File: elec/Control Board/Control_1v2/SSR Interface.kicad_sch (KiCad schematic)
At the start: 21 parts, among them J11 Screw_Terminal_01x02, Q601 BSS138

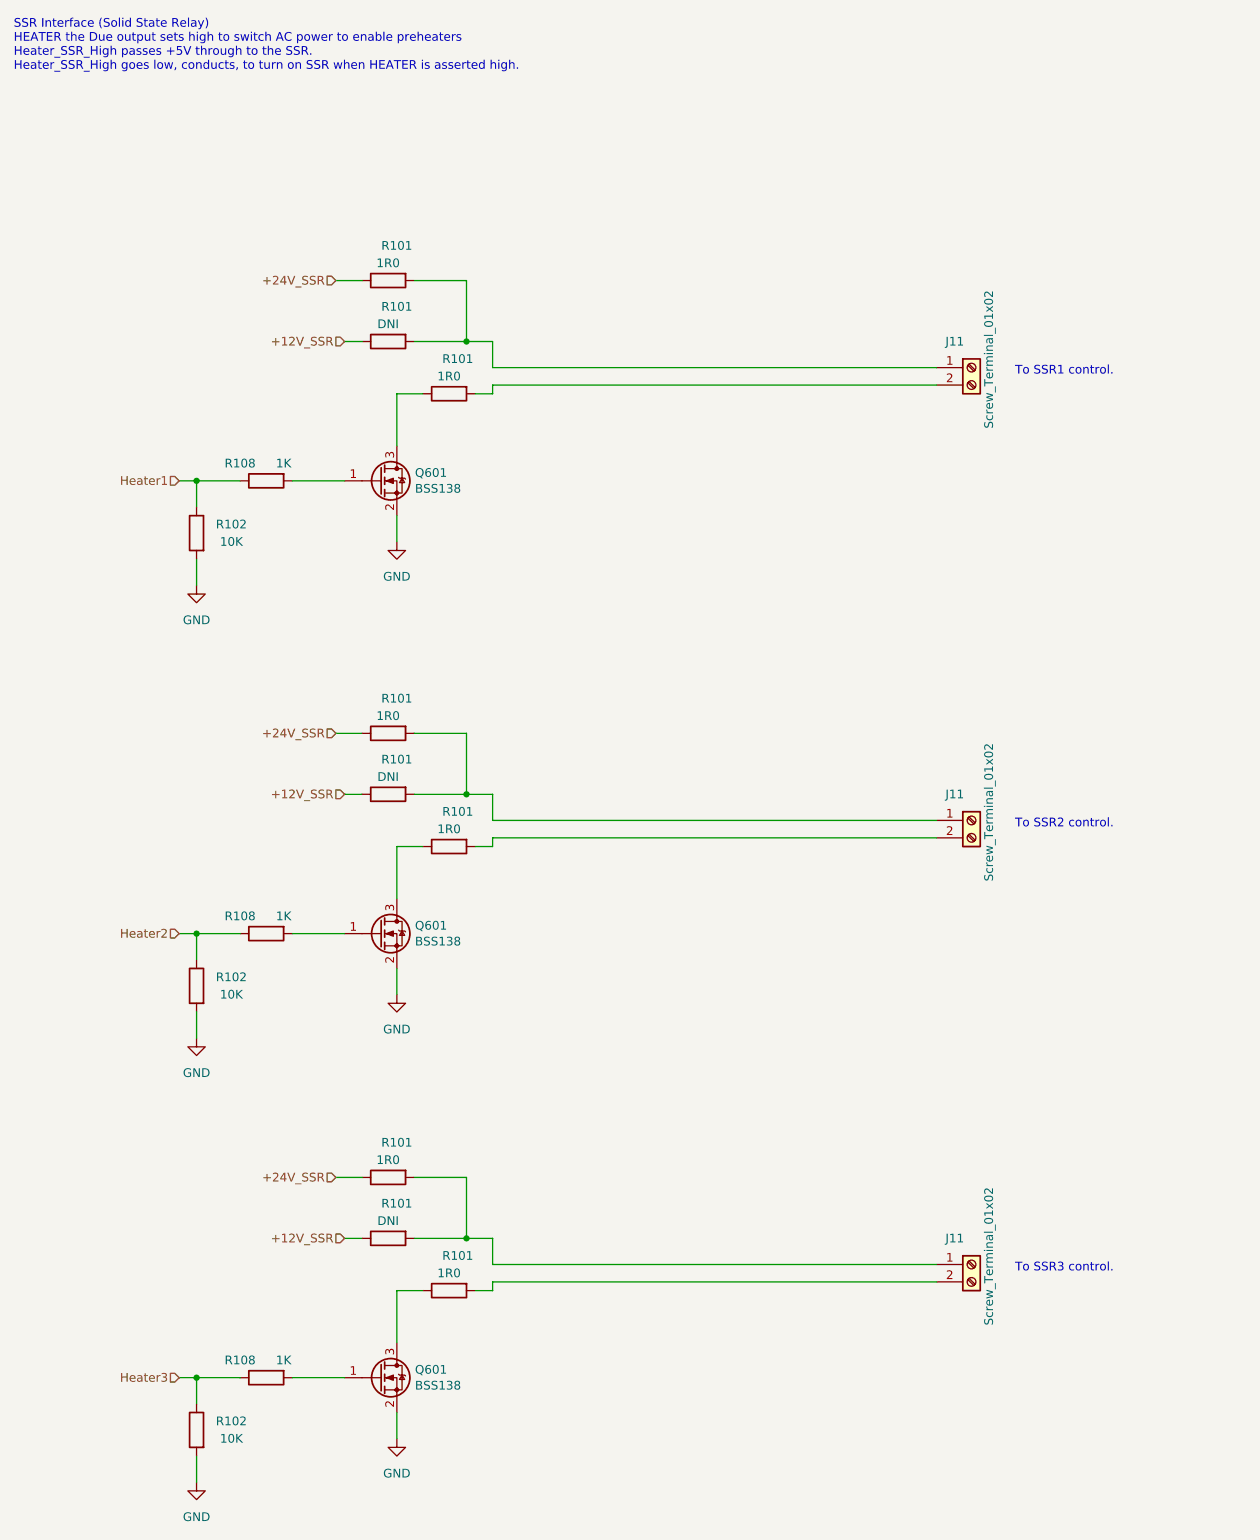
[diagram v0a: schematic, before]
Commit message: Update Control_1v2.kicad_sch for correct JLCPCB part number on JST 2 pin XH Connector. Wire up J30 as connector for OEDCS Fan.
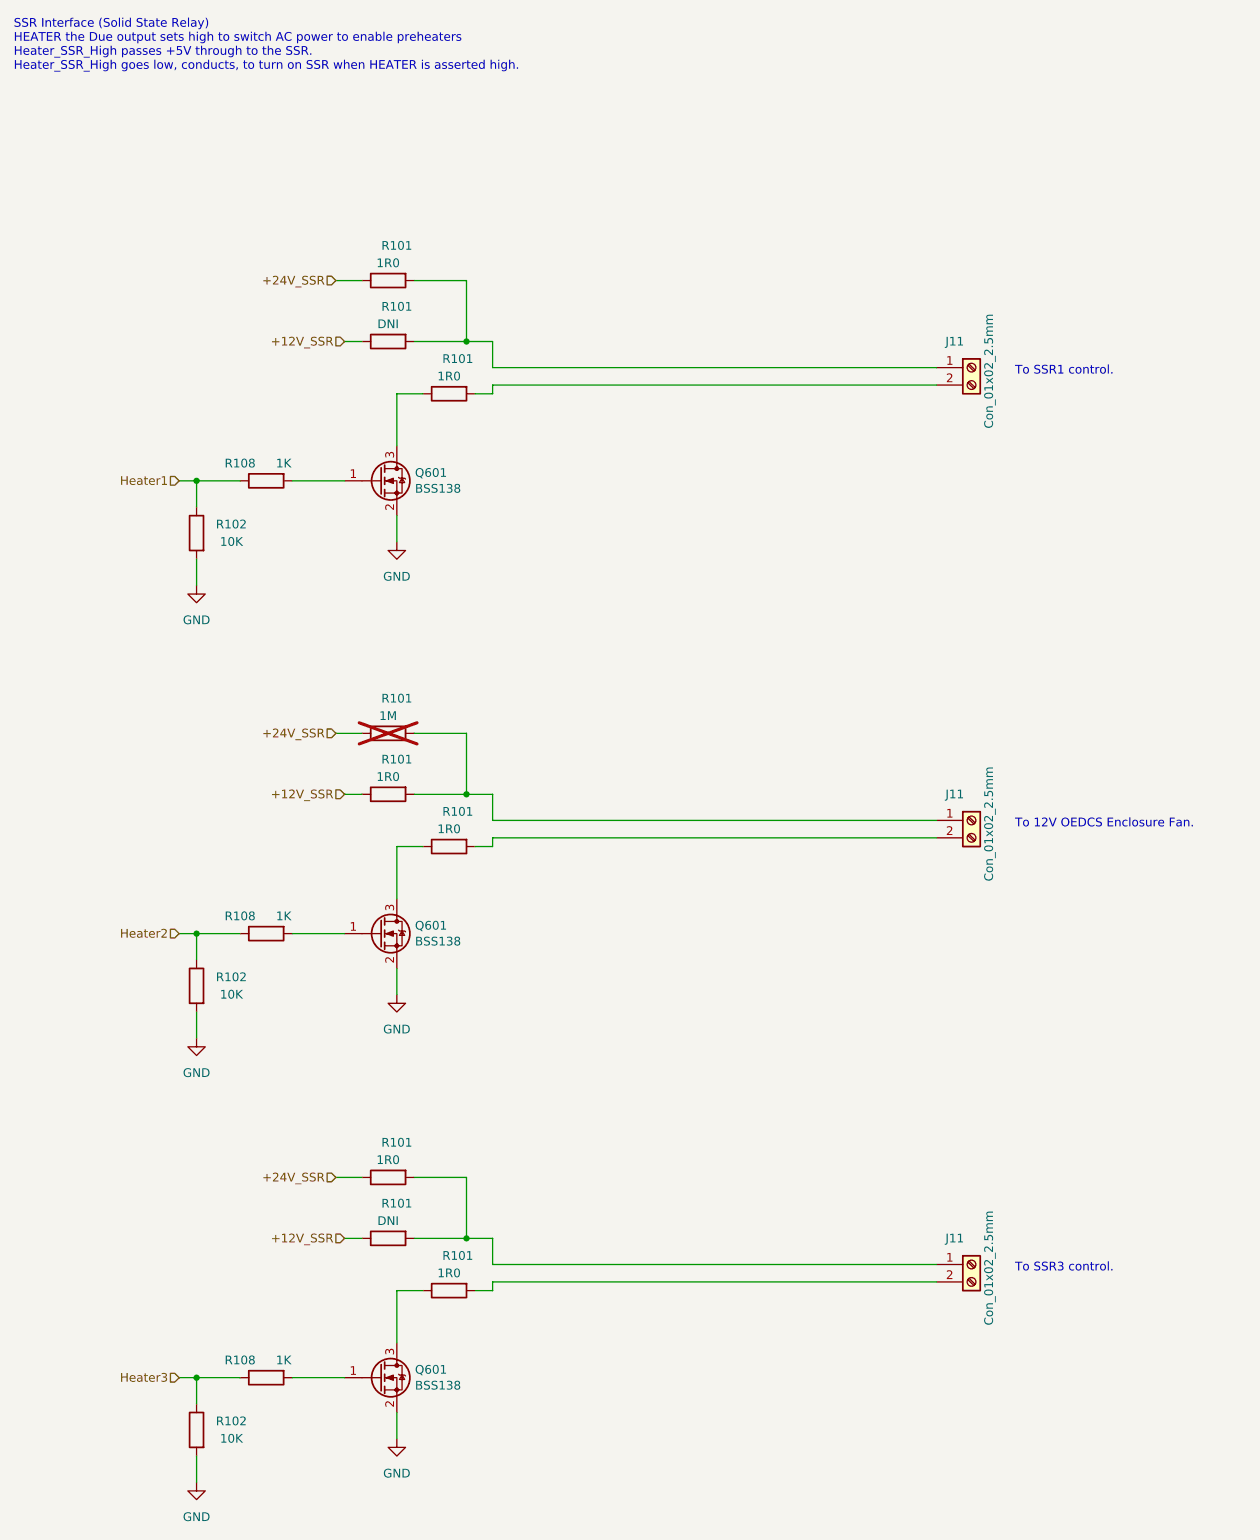
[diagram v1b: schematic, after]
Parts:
- J11: value Screw_Terminal_01x02 -> Con_01x02_2.5mm; footprint TerminalBlock_TE-Connectivity:TerminalBlock_TE_282834-2_1x02_P2.54mm_Horizontal -> Connector_JST:JST_XH_B2B-XH-AM_1x02_P2.50mm_Vertical; Cost 0.1537 -> 0.2156; MPN DB125-2.54-2P-GN-S -> B2B-XH-A-GU; Manufacturer DIBO -> JST
- R101: value DNI -> 1R0; Distributor 1 (none) -> JLCPCB; Distributor 1 PN (none) -> C269434
- R101: value 1R0 -> 1M; Distributor 1 PN C269434 -> (none); now not fitted
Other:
- note added: "To 12V OEDCS Enclosure Fan."
- note removed: "To SSR2 control."
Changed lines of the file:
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@@
     )
   )
-  (text "To SSR2 control." (at 210.82 151.13 0)
+  (text "To 12V OEDCS Enclosure Fan." (at 210.82 151.13 0)
     (effects (font (size 1.27 1.27)) (justify left bottom))
   )
@@
       (effects (font (size 1.27 1.27)) (justify left))
     )
-    (property "Value" "Screw_Terminal_01x02" (at 207.01 92.71 90)
+    (property "Value" "Con_01x02_2.5mm" (at 207.01 92.71 90)
       (effects (font (size 1.27 1.27)) (justify left))
     )
-    (property "Footprint" "TerminalBlock_TE-Connectivity:TerminalBlock_TE_282834-2_1x02_P2.54mm_Horizontal" (at 204.47 83.82 0)
+    (property "Footprint" "Connector_JST:JST_XH_B2B-XH-AM_1x02_P2.50mm_Vertical" (at 204.47 83.82 0)
       (effects (font (size 1.27 1.27)) hide)
     )
@@
       (effects (font (size 1.27 1.27)) hide)
     )
-    (property "Cost" "0.1537" (at 204.47 83.82 0)
-      (effects (font (size 1.27 1.27)) hide)
-    )
-    (property "Description" "1x2P XH 1 2.5mm 2 Brass Plugin,P=2.5mm Wire To Board / Wire To Wire Connector ROHS" (at 204.47 83.82 0)
+    (property "Cost" "0.2156" (at 204.47 83.82 0)
+      (effects (font (size 1.27 1.27)) hide)
+    )
+    (property "Description" "1x2P 2P XH Gold 2 -25℃~+85℃ 3A 1 2.5mm Brass Direct Insert Plugin,P=2.5mm Wire To Board Connector ROHS" (at 204.47 83.82 0)
       (effects (font (size 1.27 1.27)) hide)
     )
@@
       (effects (font (size 1.27 1.27)) hide)
     )
-    (property "MPN" "DB125-2.54-2P-GN-S" (at 204.47 83.82 0)
-      (effects (font (size 1.27 1.27)) hide)
-    )
-    (property "Manufacturer" "DIBO" (at 204.47 83.82 0)
+    (property "MPN" "B2B-XH-A-GU" (at 204.47 83.82 0)
+      (effects (font (size 1.27 1.27)) hide)
+    )
+    (property "Manufacturer" "JST" (at 204.47 83.82 0)
       (effects (font (size 1.27 1.27)) hide)
     )
@@
       (effects (font (size 1.27 1.27)))
     )
-    (property "Value" "DNI" (at 119.38 143.51 90)
+    (property "Value" "1R0" (at 119.38 143.51 90)
       (effects (font (size 1.27 1.27)))
     )
@@
       (effects (font (size 1.27 1.27)) hide)
     )
-    (property "Distributor 1" "" (at 119.38 146.05 90)
-      (effects (font (size 1.27 1.27)) hide)
-    )
-    (property "Distributor 1 PN" "" (at 119.38 146.05 90)
+    (property "Distributor 1" "JLCPCB" (at 119.38 146.05 90)
+      (effects (font (size 1.27 1.27)) hide)
+    )
+    (property "Distributor 1 PN" "C269434" (at 119.38 146.05 90)
       (effects (font (size 1.27 1.27)) hide)
     )
@@
       (effects (font (size 1.27 1.27)) (justify left))
     )
-    (property "Value" "Screw_Terminal_01x02" (at 207.01 158.75 90)
+    (property "Value" "Con_01x02_2.5mm" (at 207.01 158.75 90)
       (effects (font (size 1.27 1.27)) (justify left))
     )
-    (property "Footprint" "TerminalBlock_TE-Connectivity:TerminalBlock_TE_282834-2_1x02_P2.54mm_Horizontal" (at 204.47 149.86 0)
+    (property "Footprint" "Connector_JST:JST_XH_B2B-XH-AM_1x02_P2.50mm_Vertical" (at 204.47 149.86 0)
       (effects (font (size 1.27 1.27)) hide)
     )
@@
       (effects (font (size 1.27 1.27)) hide)
     )
-    (property "Cost" "0.1537" (at 204.47 149.86 0)
-      (effects (font (size 1.27 1.27)) hide)
-    )
-    (property "Description" "1x2P XH 1 2.5mm 2 Brass Plugin,P=2.5mm Wire To Board / Wire To Wire Connector ROHS" (at 204.47 149.86 0)
+    (property "Cost" "0.2156" (at 204.47 149.86 0)
+      (effects (font (size 1.27 1.27)) hide)
+    )
+    (property "Description" "1x2P 2P XH Gold 2 -25℃~+85℃ 3A 1 2.5mm Brass Direct Insert Plugin,P=2.5mm Wire To Board Connector ROHS" (at 204.47 149.86 0)
       (effects (font (size 1.27 1.27)) hide)
     )
@@
       (effects (font (size 1.27 1.27)) hide)
     )
-    (property "MPN" "DB125-2.54-2P-GN-S" (at 204.47 149.86 0)
-      (effects (font (size 1.27 1.27)) hide)
-    )
-    (property "Manufacturer" "DIBO" (at 204.47 149.86 0)
+    (property "MPN" "B2B-XH-A-GU" (at 204.47 149.86 0)
+      (effects (font (size 1.27 1.27)) hide)
+    )
+    (property "Manufacturer" "JST" (at 204.47 149.86 0)
       (effects (font (size 1.27 1.27)) hide)
     )
@@
   )
   (symbol (lib_id "Device:R") (at 119.38 137.16 90) (mirror x) (unit 1)
-    (in_bom yes) (on_board yes) (dnp no)
+    (in_bom yes) (on_board yes) (dnp yes)
     (property "Reference" "R101" (at 120.65 132.08 90)
       (effects (font (size 1.27 1.27)))
     )
-    (property "Value" "1R0" (at 119.38 134.62 90)
+    (property "Value" "1M" (at 119.38 134.62 90)
       (effects (font (size 1.27 1.27)))
     )
@@
       (effects (font (size 1.27 1.27)) hide)
     )
-    (property "Distributor 1 PN" "C269434" (at 119.38 137.16 90)
+    (property "Distributor 1 PN" "" (at 119.38 137.16 90)
       (effects (font (size 1.27 1.27)) hide)
     )
@@
       (effects (font (size 1.27 1.27)) hide)
     )
-    (property "Description" "0.1W ±5% 1Ω 0603 Chip Resistor - Surface Mount ROHS" (at 119.38 137.16 0)
+    (property "Description" "" (at 119.38 137.16 0)
       (effects (font (size 1.27 1.27)) hide)
     )
@@
       (effects (font (size 1.27 1.27)) (justify left))
     )
-    (property "Value" "Screw_Terminal_01x02" (at 207.01 223.52 90)
+    (property "Value" "Con_01x02_2.5mm" (at 207.01 223.52 90)
       (effects (font (size 1.27 1.27)) (justify left))
     )
-    (property "Footprint" "TerminalBlock_TE-Connectivity:TerminalBlock_TE_282834-2_1x02_P2.54mm_Horizontal" (at 204.47 214.63 0)
+    (property "Footprint" "Connector_JST:JST_XH_B2B-XH-AM_1x02_P2.50mm_Vertical" (at 204.47 214.63 0)
       (effects (font (size 1.27 1.27)) hide)
     )
@@
       (effects (font (size 1.27 1.27)) hide)
     )
-    (property "Cost" "0.1537" (at 204.47 214.63 0)
-      (effects (font (size 1.27 1.27)) hide)
-    )
-    (property "Description" "1x2P XH 1 2.5mm 2 Brass Plugin,P=2.5mm Wire To Board / Wire To Wire Connector ROHS" (at 204.47 214.63 0)
+    (property "Cost" "0.2156" (at 204.47 214.63 0)
+      (effects (font (size 1.27 1.27)) hide)
+    )
+    (property "Description" "1x2P 2P XH Gold 2 -25℃~+85℃ 3A 1 2.5mm Brass Direct Insert Plugin,P=2.5mm Wire To Board Connector ROHS" (at 204.47 214.63 0)
       (effects (font (size 1.27 1.27)) hide)
     )
@@
       (effects (font (size 1.27 1.27)) hide)
     )
-    (property "MPN" "DB125-2.54-2P-GN-S" (at 204.47 214.63 0)
-      (effects (font (size 1.27 1.27)) hide)
-    )
-    (property "Manufacturer" "DIBO" (at 204.47 214.63 0)
-      (effects (font (size 1.27 1.27)) hide)
-    )
+    (property "MPN" "B2B-XH-A-GU" (at 204.47 214.63 0)
+      (effects (font (size 1.27 1.27)) hide)
+    )
+    (property "Manufacturer" "JST" (at 204.47 214.63 0)
+      (effects (font (size 1.27 1.27)) hide)
+    )

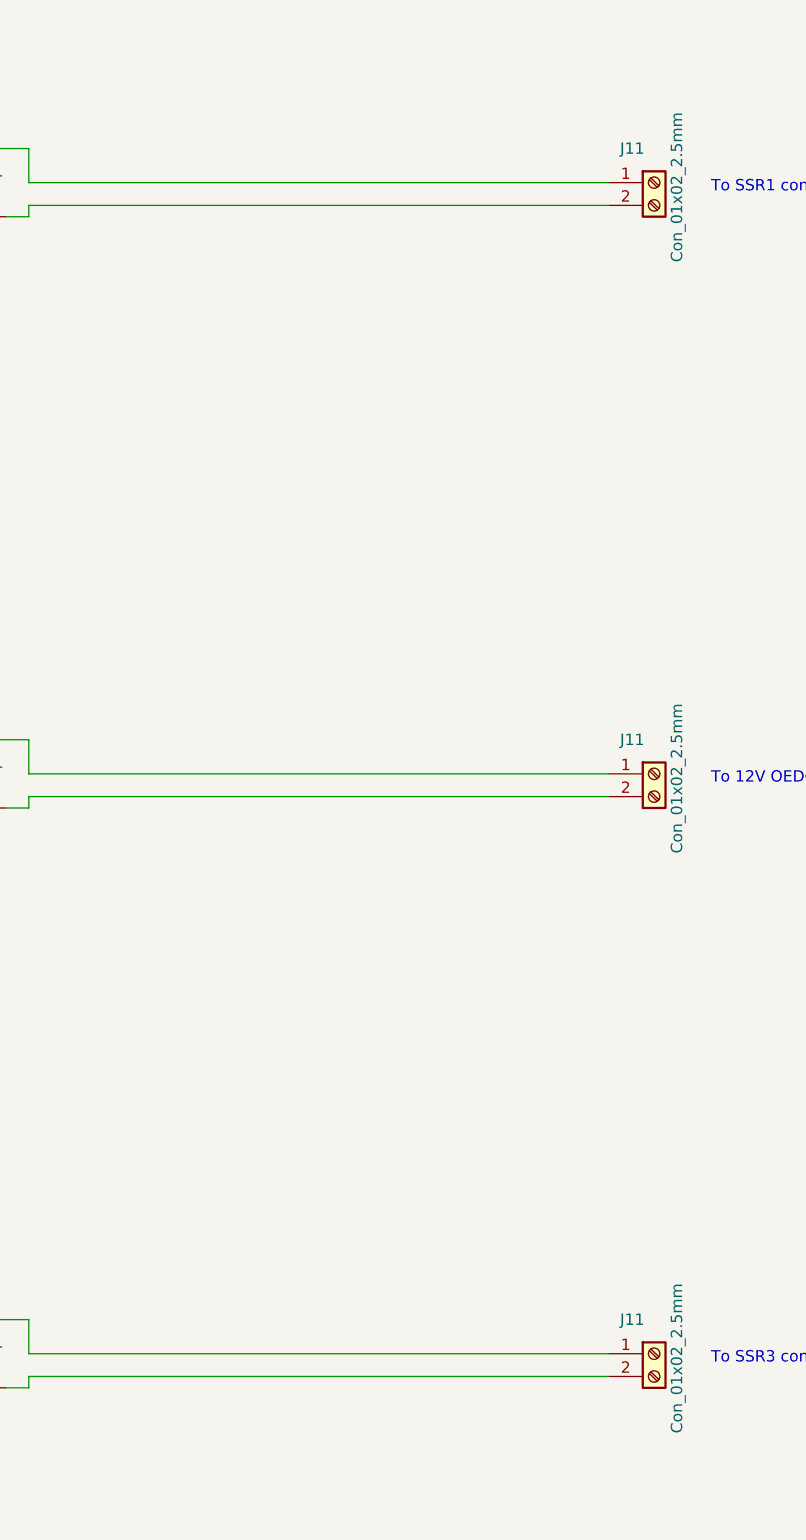
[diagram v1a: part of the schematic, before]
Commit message: PCB V1.2. Routing with out errors.
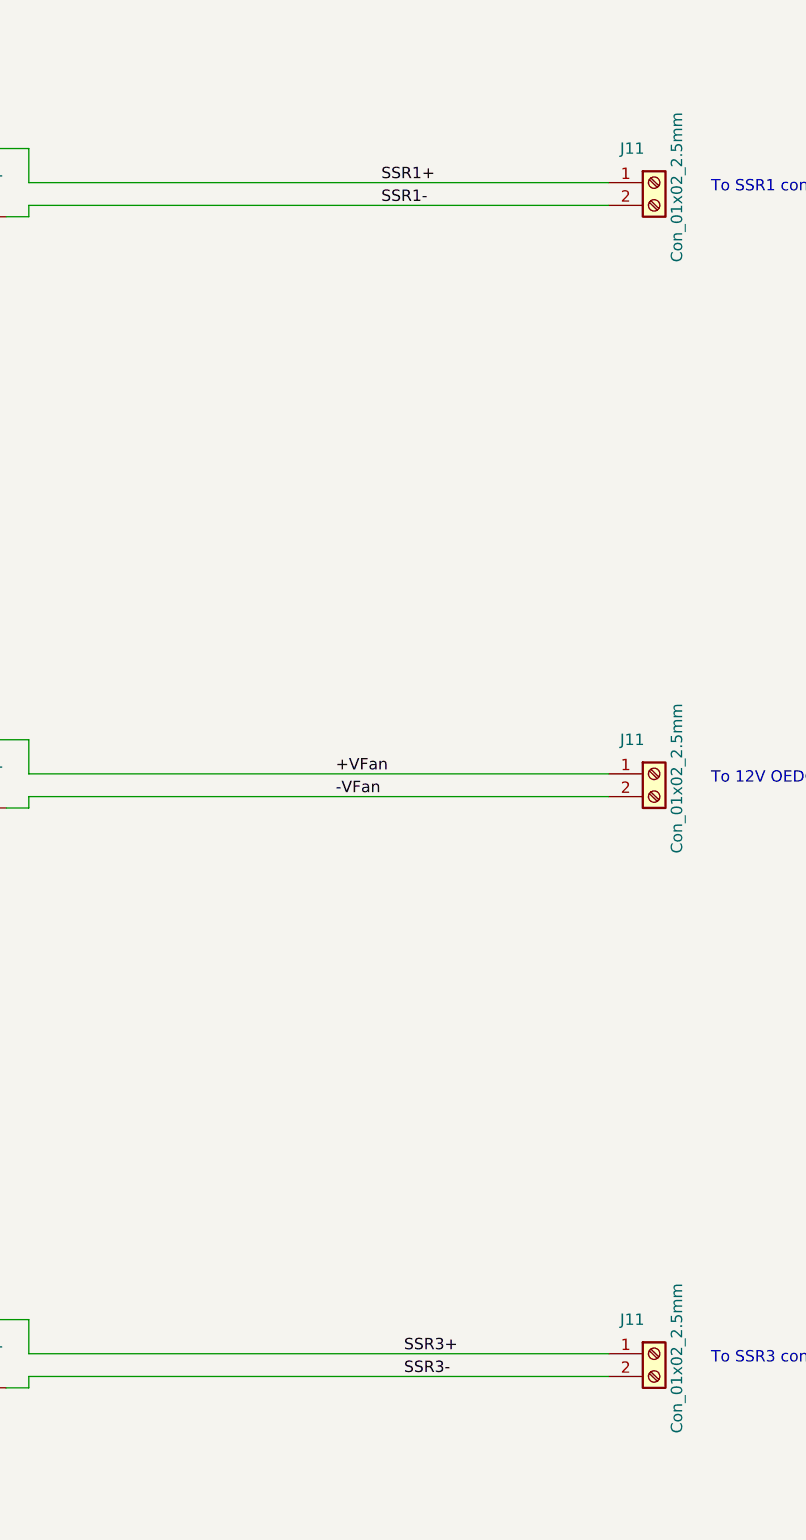
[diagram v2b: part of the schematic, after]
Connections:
- net SSR1+: now reaches J11.1 (Pin_1), R101.2, R101.2
- net SSR1-: now reaches J11.2 (Pin_2), R101.2
- net -VFan: now reaches J11.2 (Pin_2), R101.2
- net +VFan: now reaches J11.1 (Pin_1), R101.2, R101.2
- net SSR3+: now reaches J11.1 (Pin_1), R101.2, R101.2
- net SSR3-: now reaches J11.2 (Pin_2), R101.2
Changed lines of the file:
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@@
+    (effects (font (size 1.27 1.27)) (justify left bottom))
+  )
+  (label "SSR1+" (at 173.99 83.82 0) (fields_autoplaced)
+    (effects (font (size 1.27 1.27)) (justify left bottom))
+  )
+  (label "SSR3-" (at 176.53 217.17 0) (fields_autoplaced)
+    (effects (font (size 1.27 1.27)) (justify left bottom))
+  )
+  (label "-VFan" (at 168.91 152.4 0) (fields_autoplaced)
+    (effects (font (size 1.27 1.27)) (justify left bottom))
+  )
+  (label "SSR1-" (at 173.99 86.36 0) (fields_autoplaced)
+    (effects (font (size 1.27 1.27)) (justify left bottom))
+  )
+  (label "+VFan" (at 168.91 149.86 0) (fields_autoplaced)
+    (effects (font (size 1.27 1.27)) (justify left bottom))
+  )
+  (label "SSR3+" (at 176.53 214.63 0) (fields_autoplaced)
     (effects (font (size 1.27 1.27)) (justify left bottom))
   )

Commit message: Add a 3D model for the JHT connector B2B-XH-A-GU.
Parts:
- J11: footprint Connector_JST:JST_XH_B2B-XH-AM_1x02_P2.50mm_Vertical -> PubInv_KiCad_PCB:JST_XH_B2B-XH-AM_1x02_P2.50mm_Vertical
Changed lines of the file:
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@@
       (effects (font (size 1.27 1.27)) (justify left))
     )
-    (property "Footprint" "Connector_JST:JST_XH_B2B-XH-AM_1x02_P2.50mm_Vertical" (at 204.47 83.82 0)
+    (property "Footprint" "PubInv_KiCad_PCB:JST_XH_B2B-XH-AM_1x02_P2.50mm_Vertical" (at 204.47 83.82 0)
       (effects (font (size 1.27 1.27)) hide)
     )
@@
       (effects (font (size 1.27 1.27)) (justify left))
     )
-    (property "Footprint" "Connector_JST:JST_XH_B2B-XH-AM_1x02_P2.50mm_Vertical" (at 204.47 149.86 0)
+    (property "Footprint" "PubInv_KiCad_PCB:JST_XH_B2B-XH-AM_1x02_P2.50mm_Vertical" (at 204.47 149.86 0)
       (effects (font (size 1.27 1.27)) hide)
     )
@@
       (effects (font (size 1.27 1.27)) (justify left))
     )
-    (property "Footprint" "Connector_JST:JST_XH_B2B-XH-AM_1x02_P2.50mm_Vertical" (at 204.47 214.63 0)
-      (effects (font (size 1.27 1.27)) hide)
-    )
+    (property "Footprint" "PubInv_KiCad_PCB:JST_XH_B2B-XH-AM_1x02_P2.50mm_Vertical" (at 204.47 214.63 0)
+      (effects (font (size 1.27 1.27)) hide)
+    )
